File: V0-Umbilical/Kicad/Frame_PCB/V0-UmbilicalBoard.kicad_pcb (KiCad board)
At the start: 2 copper layers, 122 x 37 mm, 16 parts, among them J1 Conn_02x08_Odd_Even, J10 Neopixel Strip 1, J11 Neopixel Strip 1, J12 Neopixel Out, J2 Motor, J3 Hotend Fan, J4 Part Cooling Fan, J5 Heater, J6 Thermistor, J7 X-Endstop, J8 Chamber Thermistor, J9 Neopixel (from controller)

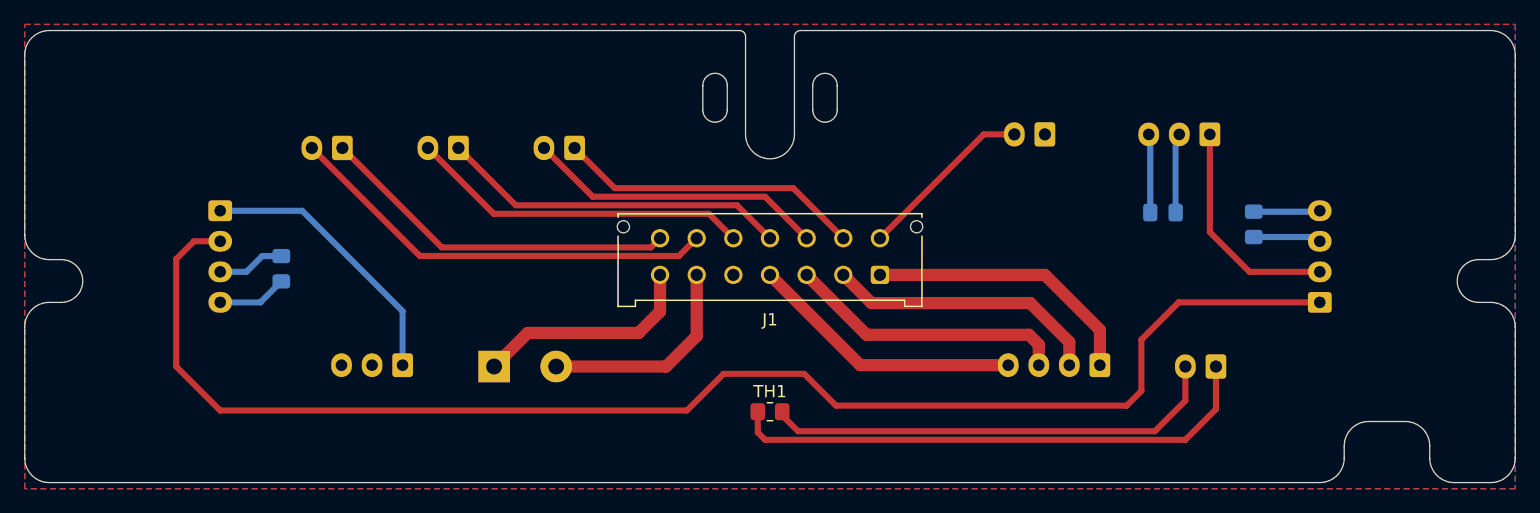
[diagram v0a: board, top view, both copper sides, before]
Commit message: Update to Rev A.1
- Fix incidental connection between endstop ground and neopixel ground which could cause issues if the controller-to-frame_pcb wires weren't correct.
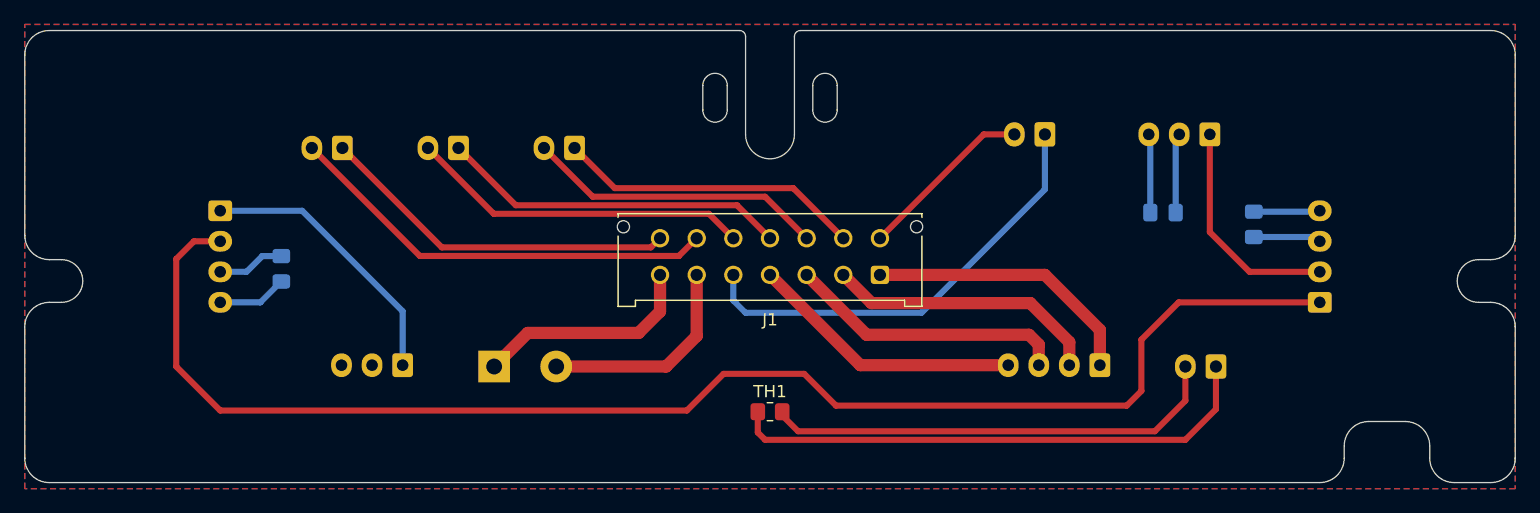
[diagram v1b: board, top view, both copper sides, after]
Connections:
- C1 pad 2: Ground -> Neo_Ground
- C2 pad 2: Ground -> Neo_Ground
- C3 pad 2: Ground -> Neo_Ground
- J1 pad 5: Ground -> Net-(J7-Pad1)
- J10 pad 4: Ground -> Neo_Ground
- J11 pad 4: Ground -> Neo_Ground
- J12 pad 3: Ground -> Neo_Ground
- J7 pad 1: Ground -> Net-(J7-Pad1)
- J9 pad 3: Ground -> Neo_Ground
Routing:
- net Net-(J7-Pad1): track 0.00 -> 36.7 mm
- net Neo_Ground: track 0.00 -> 17.6 mm
- net Ground: track 17.6 -> 0.00 mm
- added copper zone on B.Cu, net Neo_Ground
- removed copper zone on B.Cu, net Ground
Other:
- net class Default removed
- board text added: "V0 Umbilical Breakout Board Rev A.1 - 5/14/22 T. Abraham"
- board text removed: "V0 Umbilical Breakout Board Rev A - 4/20/21 T. Abraham"

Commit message: Fix KiCad 6 model errors and add images (#174)
Fix Kicad 6 model linking errors and update images with Rev A.1 traces.
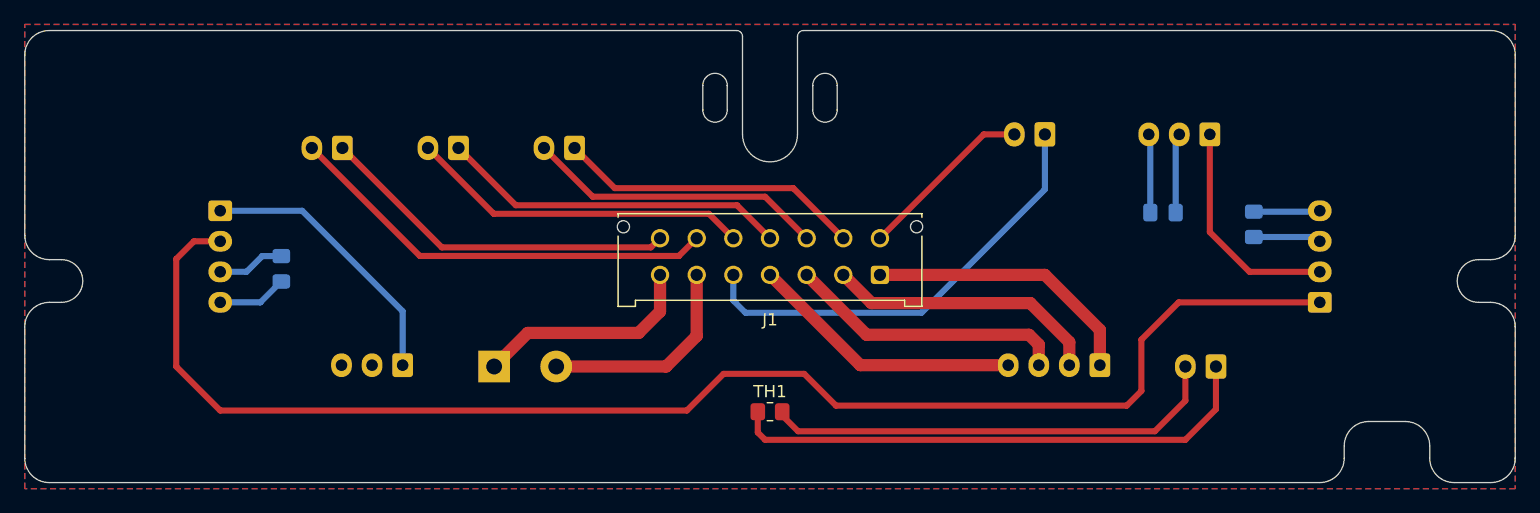
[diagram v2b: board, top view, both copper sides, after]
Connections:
- net DataOut2 renamed DataIn3
- net Neo_Ground renamed GND
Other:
- outline, holes or cut-outs redrawn
